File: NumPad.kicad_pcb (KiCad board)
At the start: 2 copper layers, 79.4 x 115.1 mm, 50 parts, among them J1 USB_B_Micro, K1 numlk, K10 5, K11 6, K12 enter, K13 1, K14 2, K15 3, K16 0, K17 .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

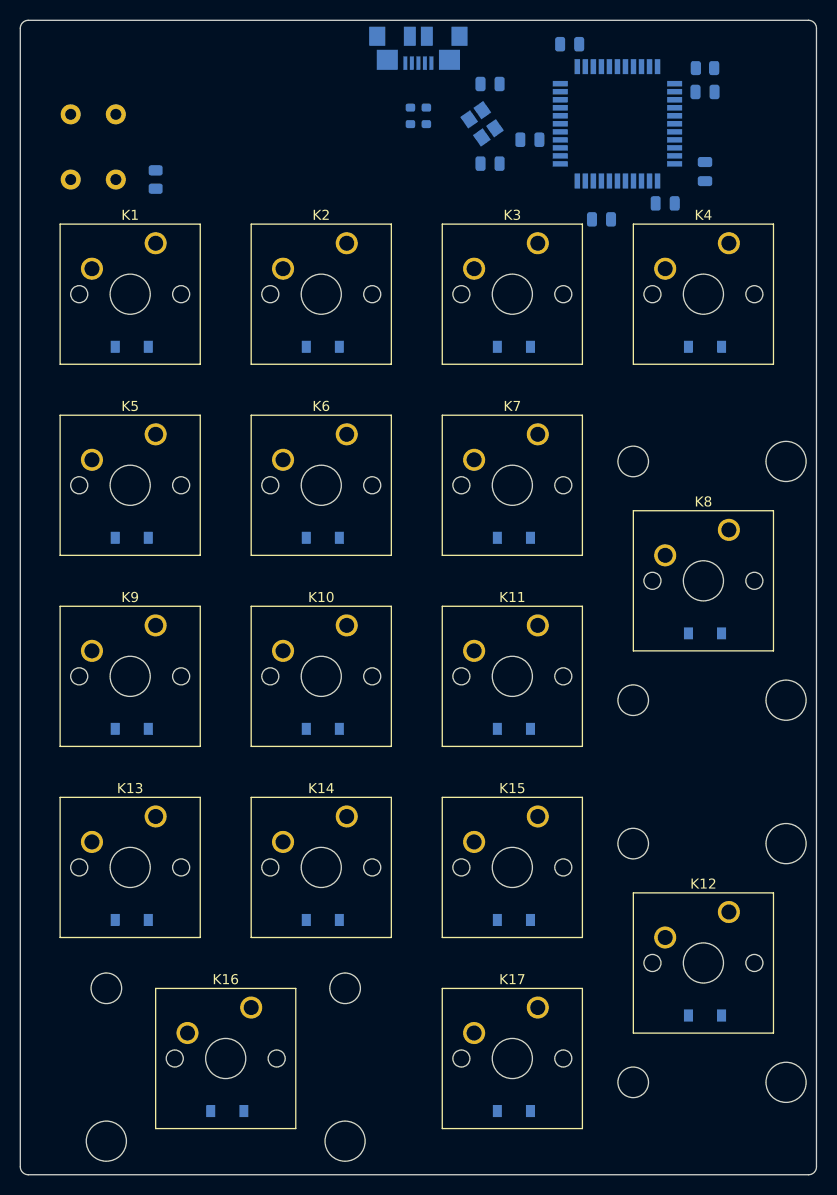
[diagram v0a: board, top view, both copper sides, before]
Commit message: Planos de tierra y vcc añadidos
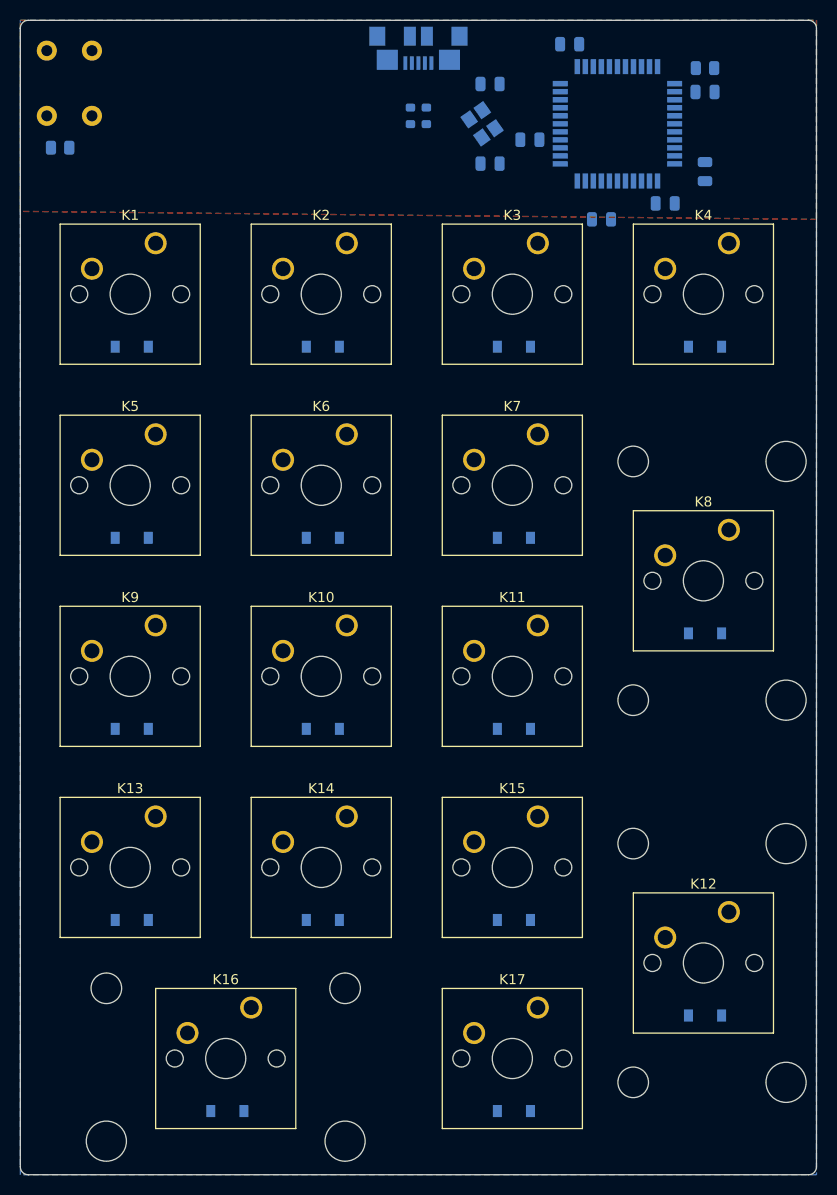
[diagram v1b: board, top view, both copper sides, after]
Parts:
- moved R1 10.0 mm to (82.5, 62.7), turned to 180 degrees
- moved SW1 6.78 mm to (85.7, 59.5)
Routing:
- added copper zone on B.Cu, net GND
- added copper zone on F.Cu, net VCC

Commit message: Plugins añadidos y columnadas enrutadas
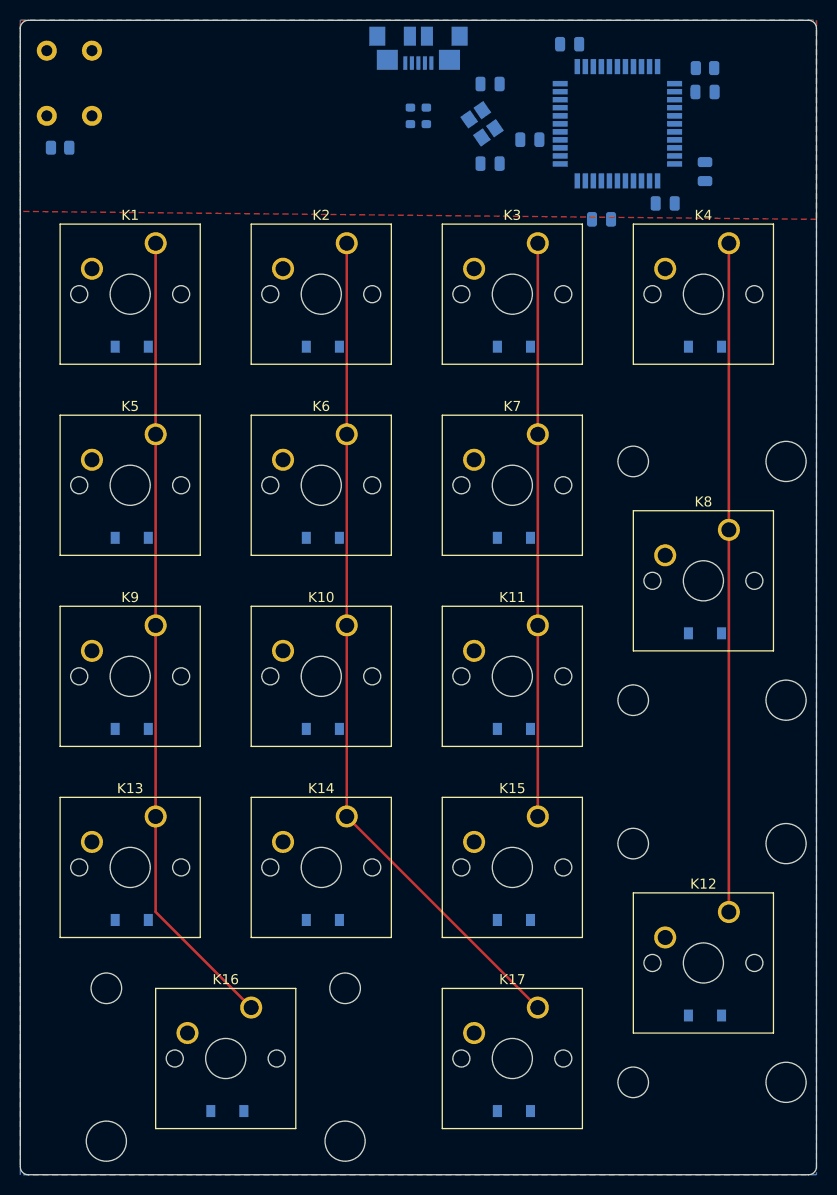
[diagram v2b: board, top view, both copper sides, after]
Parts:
- turned D1 to 180 degrees
- turned D10 to 180 degrees
- turned D11 to 180 degrees
- turned D12 to 180 degrees
- turned D13 to 180 degrees
- turned D14 to 180 degrees
- turned D15 to 180 degrees
- turned D16 to 180 degrees
- turned D17 to 180 degrees
- turned D2 to 180 degrees
- turned D3 to 180 degrees
- turned D4 to 180 degrees
- turned D5 to 180 degrees
- turned D6 to 180 degrees
- turned D7 to 180 degrees
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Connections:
- D1 pad 1: /col1 -> row1
- D10 pad 1: /col2 -> row3
- D11 pad 1: /col3 -> row3
- D12 pad 1: /col4 -> row3
- D13 pad 1: /col1 -> row4
- D14 pad 1: /col2 -> row4
- D15 pad 1: /col3 -> row4
- D16 pad 1: /col1 -> row5
- D17 pad 1: /col3 -> row5
- D2 pad 1: /col2 -> row1
- D3 pad 1: /col3 -> row1
- D4 pad 1: /col4 -> row1
- D5 pad 1: /col1 -> row2
- D6 pad 1: /col2 -> row2
- D7 pad 1: /col3 -> row2
- D8 pad 1: /col4 -> row2
- D9 pad 1: /col1 -> row3
- K1 pad 1: Net-(D1-Pad2) -> col1
- K1 pad 2: /row1 -> Net-(D1-Pad2)
- K10 pad 1: Net-(D10-Pad2) -> col2
- K10 pad 2: /row3 -> Net-(D10-Pad2)
- K11 pad 1: Net-(D11-Pad2) -> col3
- K11 pad 2: /row3 -> Net-(D11-Pad2)
- K12 pad 1: Net-(D12-Pad2) -> col4
- K12 pad 2: /row3 -> Net-(D12-Pad2)
- K13 pad 1: Net-(D13-Pad2) -> col1
- K13 pad 2: /row4 -> Net-(D13-Pad2)
- K14 pad 1: Net-(D14-Pad2) -> col2
- K14 pad 2: /row4 -> Net-(D14-Pad2)
- K15 pad 1: Net-(D15-Pad2) -> col3
- K15 pad 2: /row4 -> Net-(D15-Pad2)
- K16 pad 1: Net-(D16-Pad2) -> col1
- K16 pad 2: /row5 -> Net-(D16-Pad2)
- K17 pad 1: Net-(D17-Pad2) -> col2
- K17 pad 2: /row5 -> Net-(D17-Pad2)
- K2 pad 1: Net-(D2-Pad2) -> col2
- K2 pad 2: /row1 -> Net-(D2-Pad2)
- K3 pad 1: Net-(D3-Pad2) -> col3
- K3 pad 2: /row1 -> Net-(D3-Pad2)
- K4 pad 1: Net-(D4-Pad2) -> col4
- K4 pad 2: /row1 -> Net-(D4-Pad2)
- K5 pad 1: Net-(D5-Pad2) -> col1
- K5 pad 2: /row2 -> Net-(D5-Pad2)
- K6 pad 1: Net-(D6-Pad2) -> col2
- K6 pad 2: /row2 -> Net-(D6-Pad2)
- K7 pad 1: Net-(D7-Pad2) -> col3
- K7 pad 2: /row2 -> Net-(D7-Pad2)
- K8 pad 1: Net-(D8-Pad2) -> col4
- K8 pad 2: /row2 -> Net-(D8-Pad2)
- K9 pad 1: Net-(D9-Pad2) -> col1
- K9 pad 2: /row3 -> Net-(D9-Pad2)
- U1 pad 18: /col1 -> col1
- U1 pad 19: /col2 -> col2
- U1 pad 20: /col3 -> col3
- U1 pad 21: /col4 -> col4
- U1 pad 37: /row5 -> row5
- U1 pad 38: /row4 -> row4
- U1 pad 39: /row3 -> row3
- U1 pad 40: /row2 -> row2
- U1 pad 41: /row1 -> row1
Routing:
- net col2: track 0.00 -> 84.1 mm
- net col1: track 0.00 -> 80.1 mm
- net col4: track 0.00 -> 66.7 mm
- net col3: track 0.00 -> 57.1 mm

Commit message: Mas conexiones y correcion de errores.
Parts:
- moved C2 27.4 mm to (151.7, 56.8), turned to 0 degrees
- moved C1 26.9 mm to (151.7, 62.2), turned to 0 degrees
- moved X1 24.1 mm to (148.7, 59.4), turned to 125 degrees
- moved R2 18.2 mm to (135.2, 68.8)
- moved C8 18.1 mm to (139.8, 52.0), turned to 0 degrees
- moved C3 17.8 mm to (129.0, 65.5), turned to 180 degrees
- moved C6 10.4 mm to (143.8, 52.0), turned to 0 degrees
- moved D15 5.62 mm to (133.3, 138.8), turned to 90 degrees
- moved D5 5.62 mm to (95.2, 100.7), turned to 90 degrees
- moved D12 5.61 mm to (152.4, 148.4), turned to 90 degrees
- moved D4 5.61 mm to (152.4, 81.8), turned to 90 degrees
- moved D8 5.61 mm to (152.4, 110.3), turned to 90 degrees
- moved D1 5.61 mm to (95.2, 81.8), turned to 90 degrees
- moved D10 5.61 mm to (114.3, 119.8), turned to 90 degrees
- moved D11 5.61 mm to (133.3, 119.8), turned to 90 degrees
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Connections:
- net Net-(J1-Pad2) renamed DN
- net Net-(J1-Pad3) renamed DP
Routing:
- net row3: track 0.00 -> 79.1 mm
- net row2: track 0.00 -> 61.1 mm
- net row1: track 0.00 -> 57.1 mm
- net row4: track 0.00 -> 38.1 mm
- net row5: track 0.00 -> 29.1 mm
- net Net-(D14-Pad2): track 0.00 -> 13.0 mm
- net Net-(D13-Pad2): track 0.00 -> 13.0 mm
- net Net-(D9-Pad2): track 0.00 -> 13.0 mm
- net Net-(D8-Pad2): track 0.00 -> 13.0 mm
- net Net-(D7-Pad2): track 0.00 -> 13.0 mm
- net Net-(D6-Pad2): track 0.00 -> 13.0 mm
- net Net-(D4-Pad2): track 0.00 -> 13.0 mm
- net Net-(D3-Pad2): track 0.00 -> 13.0 mm
- net Net-(D2-Pad2): track 0.00 -> 13.0 mm
- net Net-(D11-Pad2): track 0.00 -> 13.0 mm
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- added copper zone on F.Cu, net GND
- removed copper zone on F.Cu, net VCC
